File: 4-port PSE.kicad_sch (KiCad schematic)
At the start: 23 parts, among them J1 1x7 2.54mm PV Female Header, U1 MP3924GU-Z

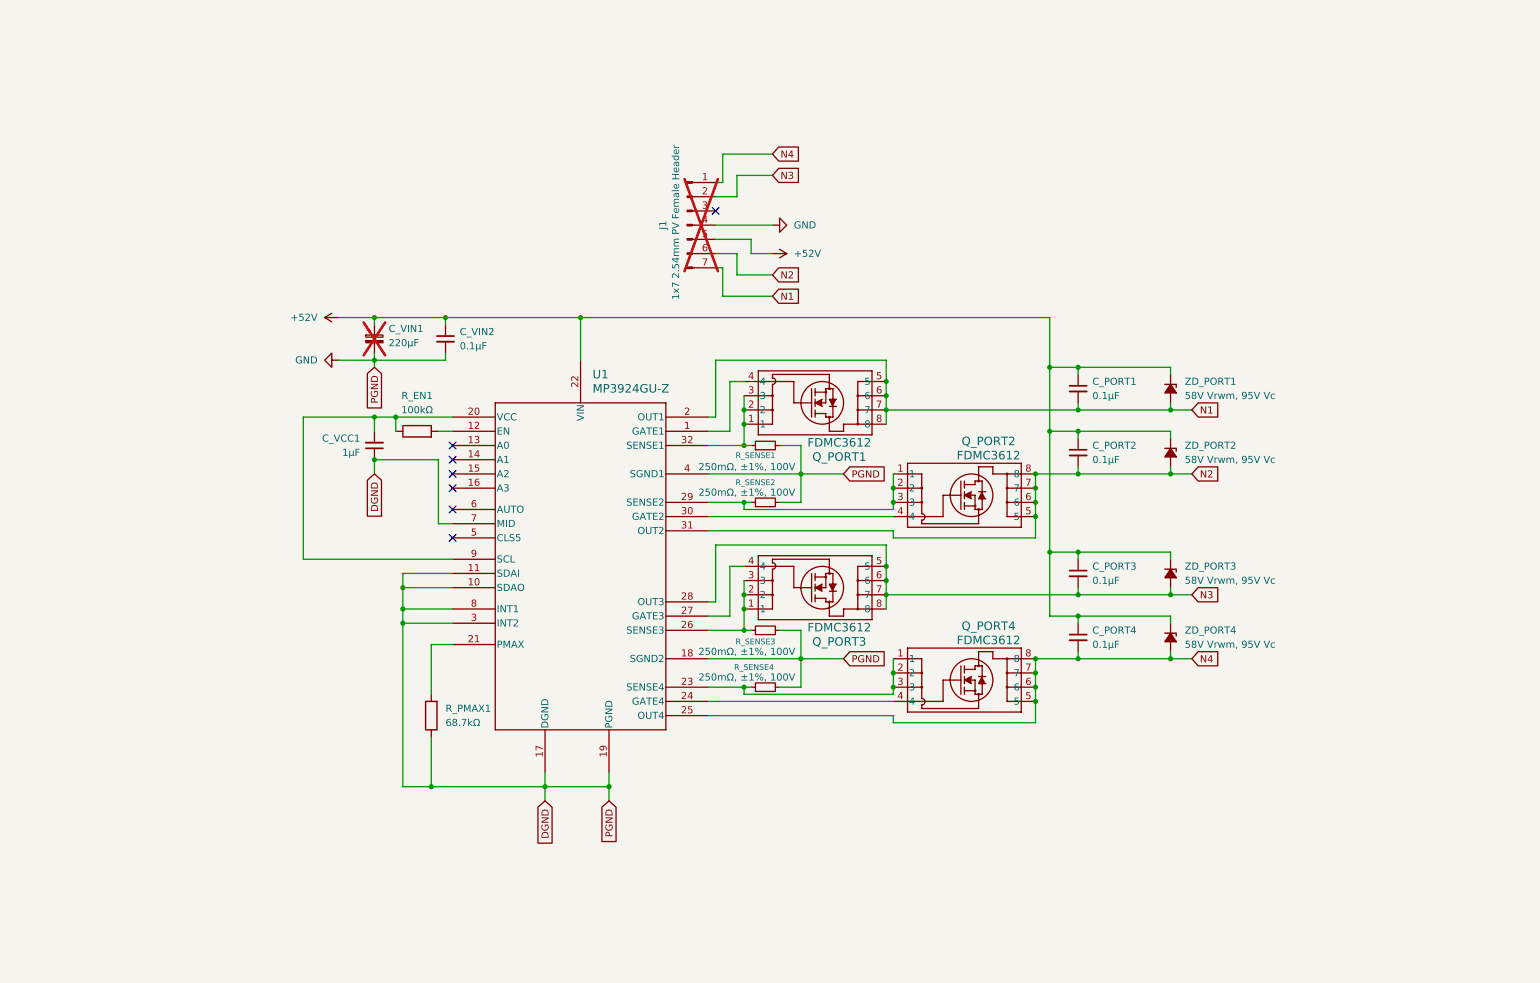
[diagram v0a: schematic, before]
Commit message: V2.0 - ESP32-C6 controlled
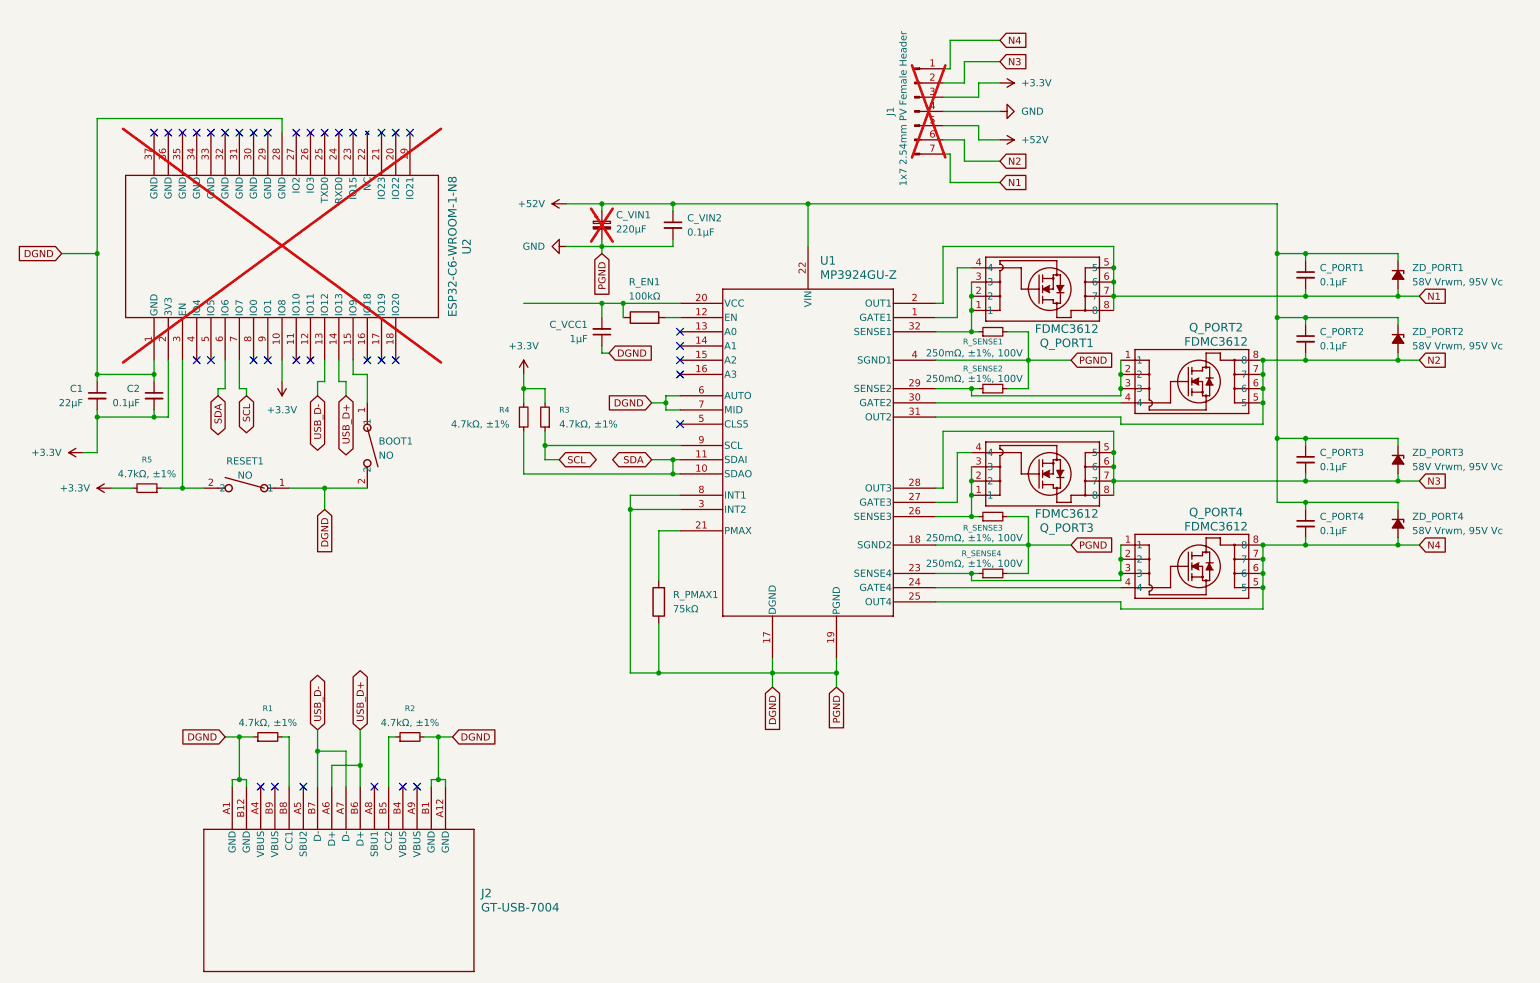
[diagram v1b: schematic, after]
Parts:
- added BOOT1, RESET1: NO, SW_TS-1088_XNP, symbol TS-1088-AR02016:TS-1088-AR02016
- added C1: 22µF, Capacitor_SMD:C_0603_1608Metric, symbol Device:C_Small
- added C2: 0.1µF, Capacitor_SMD:C_0603_1608Metric, symbol Device:C_Small
- added J2: GT-USB-7004, CONN12_B-7004_GSW, symbol GT-USB-7004:GT-USB-7004
- added R1, R2, R3, R4, R5: 4.7kΩ, ±1%, Resistor_SMD:R_0402_1005Metric, symbol Device:R_Small
- added U2: ESP32-C6-WROOM-1-N8, MOD28_ESP32-C6-WROOM-1_EXP, symbol ESP32-C6-WROOM-1:ESP32-C6-WROOM-1-N8
- C_PORT1, C_PORT2, C_PORT3, C_PORT4, C_VIN2: footprint Capacitor_SMD:C_1206_3216Metric -> Capacitor_SMD:C_0805_2012Metric
- R_EN1: footprint Resistor_SMD:R_0603_1608Metric -> Resistor_SMD:R_0402_1005Metric
- R_PMAX1: value 68.7kΩ -> 75kΩ; footprint Resistor_SMD:R_1206_3216Metric -> Resistor_SMD:R_0603_1608Metric
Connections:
- net GND: now also U1.6 (AUTO), BOOT1.2, C1.1, C2.1, J2.A1 (GND), J2.A12 (GND), J2.B1 (GND), J2.B12 (GND), R1.1, R2.2, RESET1.1, U2.1 (GND), U2.28 (GND); no longer U1.10 (SDAO), U1.11 (SDAI)
- net +3.3V: now reaches J1.3 (Pin_3)
- net +3.3V: now also C1.2, C2.2, R3.2, R4.2, R5.2, U2.10 (IO8), U2.2 (3V3)
- net at C_VCC1.2, R_EN1.1, U1.20 (VCC): no longer U1.9 (SCL)
- new net: R5.1, RESET1.2, U2.3 (EN)
- new net: J2.B5 (CC2), R2.1
- new net: J2.B8 (CC1), R1.2
- new net: BOOT1.1, U2.15 (IO9)
- new net SCL: R3.1, U1.9 (SCL), U2.7 (IO7)
- new net SDA: R4.1, U1.10 (SDAO), U1.11 (SDAI), U2.6 (IO6)
- new net USB_D+: J2.A6 (D+), J2.B6 (D+), U2.14 (IO13)
- new net USB_D-: J2.A7 (D-), J2.B7 (D-), U2.13 (IO12)
- no-connect marks 7 -> 37
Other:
- moved on the sheet: C_PORT1, C_PORT2, C_PORT3, C_PORT4, C_VCC1, C_VIN1, C_VIN2, J1, Q_PORT1, Q_PORT2, Q_PORT3, Q_PORT4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
